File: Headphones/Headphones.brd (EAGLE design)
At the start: 50 x 50 mm, 26 parts, among them U1 SI4468, Y1 30MHz

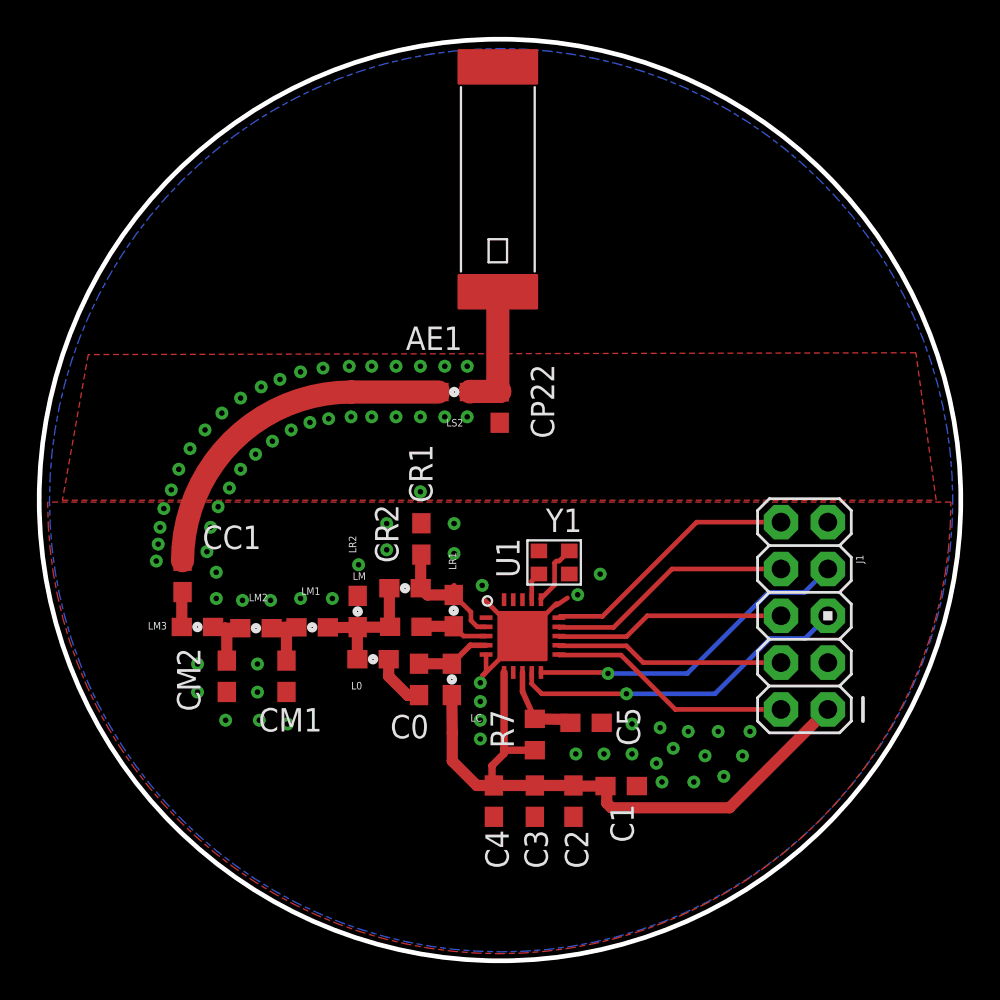
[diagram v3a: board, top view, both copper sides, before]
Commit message: Fixed antenna and transciever stop masks. Finished via placement. DRC checks out
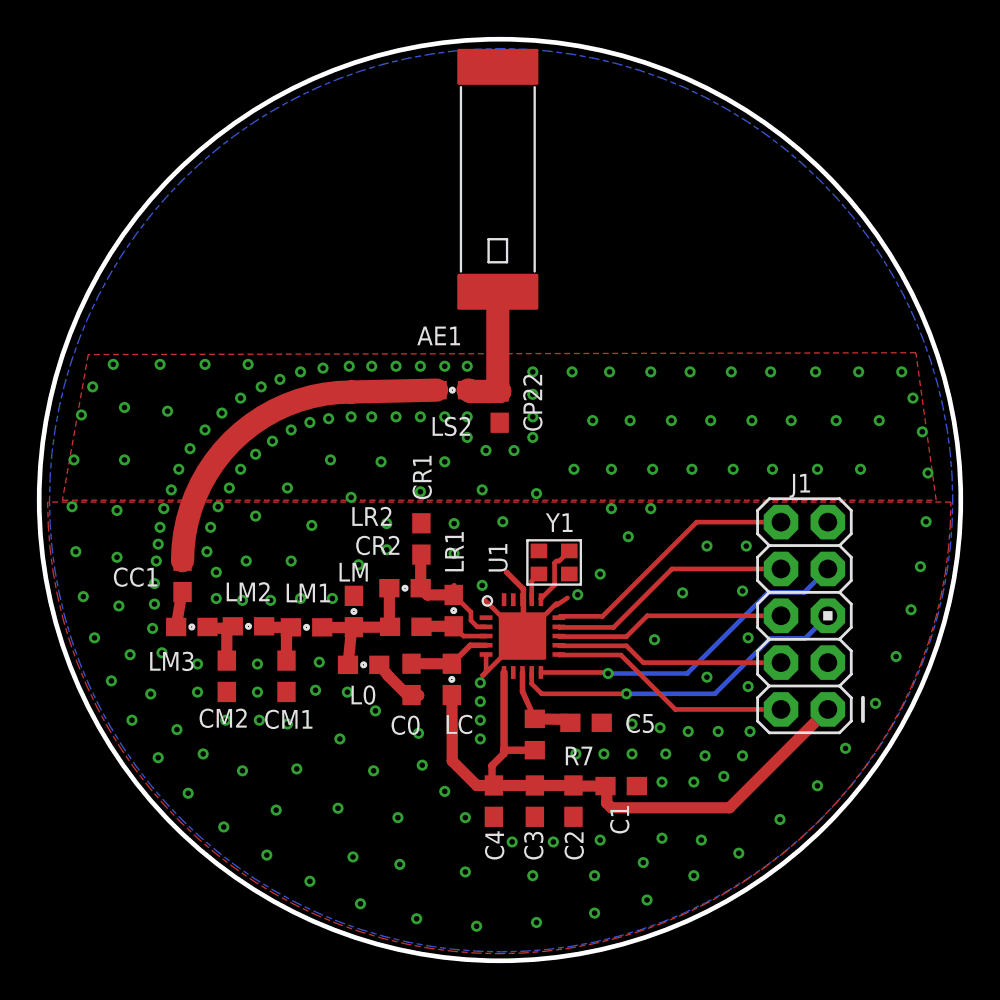
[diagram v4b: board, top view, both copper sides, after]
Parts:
- moved L0 0.59 mm to (23.6, 13.5)
- moved LM2 0.42 mm to (17.4, 15.6)
- moved C0 0.41 mm to (26.2, 12.7)
- moved LM1 0.30 mm to (20.5, 15.5)
- moved LM3 0.30 mm to (14.3, 15.5)
- moved LM 0.20 mm to (23.1, 16.4)
- moved LS2 0.14 mm to (28.5, 28.4)
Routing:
- net GND: track 7.33 -> 10.0 mm, vias 77 -> 208
- net N$6: track 7.23 -> 7.84 mm
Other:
- board text added: "3V3"
- board text added: "GND"
- board text added: "GP0"
- board text added: "GP1"
- board text added: "NIRQ"
- board text added: "NSEL"
- board text added: "SCLK"
- board text added: "SDI"
- board text added: "SDO"

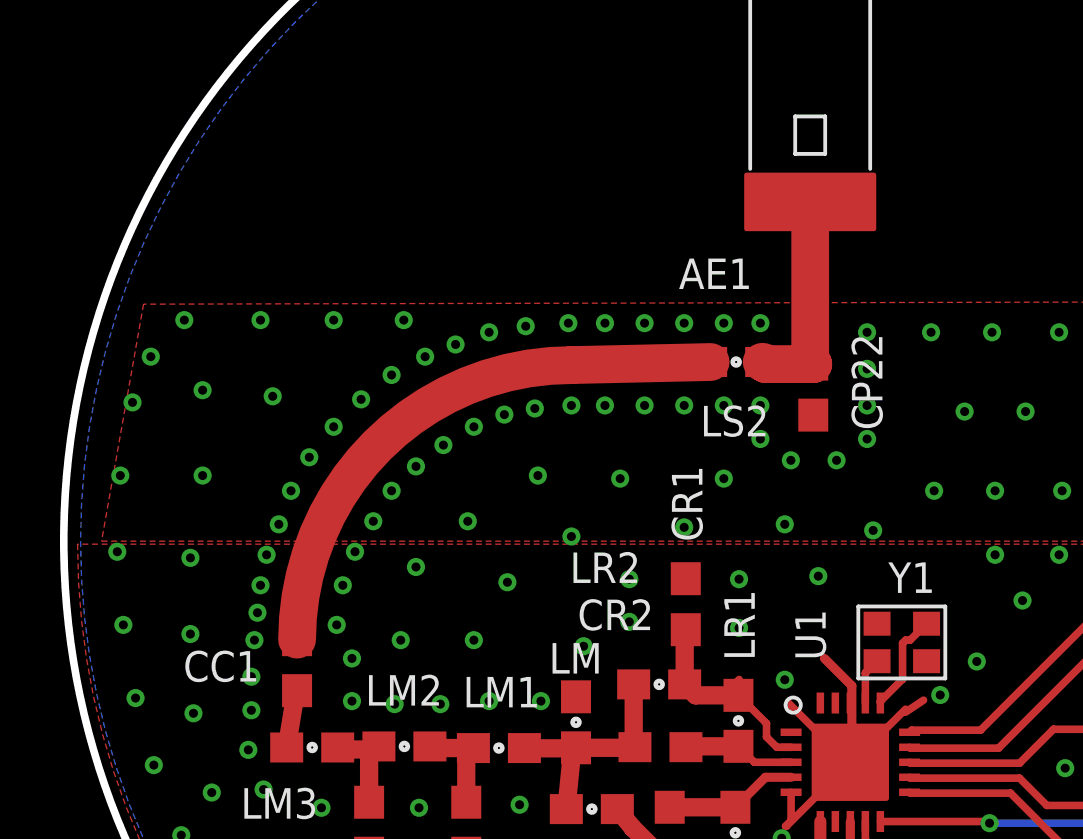
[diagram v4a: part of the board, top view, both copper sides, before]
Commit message: Minor routing changes to antenna
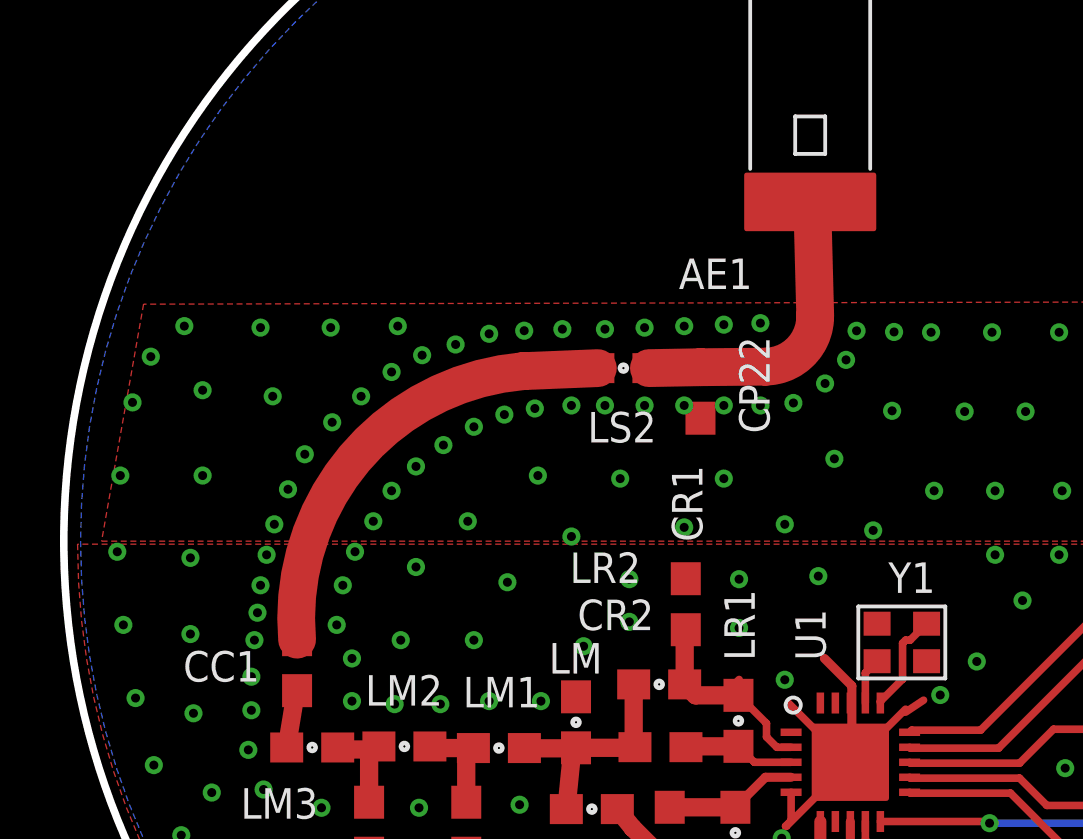
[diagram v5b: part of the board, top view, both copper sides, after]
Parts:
- moved LS2 3.76 mm to (24.7, 28.2)
- moved CP22 3.76 mm to (27.3, 27.3)
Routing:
- net N$9: track 17.6 -> 14.2 mm
- net N$13: track 7.29 -> 10.2 mm
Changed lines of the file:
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@@
 <setting verticaltext="up"/>
 </settings>
-<grid distance="4" unitdist="mil" unit="mm" style="lines" multiple="1" display="yes" altdistance="0.025" altunitdist="inch" altunit="inch"/>
+<grid distance="0.05" unitdist="mm" unit="mm" style="lines" multiple="1" display="yes" altdistance="0.025" altunitdist="inch" altunit="inch"/>
 <layers>
 <layer number="1" name="Top" color="4" fill="1" visible="yes" active="yes"/>
@@
 <attribute name="NAME" x="23.9918" y="19.004" size="1.016" layer="25" font="vector" ratio="14" rot="R180"/>
 </element>
-<element name="LS2" library="SparkFun-Passives" package="0603" value="10nH" x="28.4534" y="28.3716" smashed="yes" rot="R180">
-<attribute name="NAME" x="29.552" y="26.9096" size="1.016" layer="25" font="vector" ratio="14" rot="R180"/>
-</element>
-<element name="CP22" library="resistor" package="C0603" value="1.2pF" x="31.023" y="27.452" smashed="yes" rot="R90">
-<attribute name="NAME" x="33.328" y="26.097" size="1.016" layer="25" ratio="14" rot="R90"/>
+<element name="LS2" library="SparkFun-Passives" package="0603" value="10nH" x="24.6942" y="28.1684" smashed="yes" rot="R180">
+<attribute name="NAME" x="25.7928" y="26.7064" size="1.016" layer="25" font="vector" ratio="14" rot="R180"/>
+</element>
+<element name="CP22" library="resistor" package="C0603" value="1.2pF" x="27.2638" y="27.3488" smashed="yes" rot="R90">
+<attribute name="NAME" x="29.5688" y="25.9938" size="1.016" layer="25" ratio="14" rot="R90"/>
 </element>
 </elements>
@@
 <via x="29.2608" y="26.924" extent="1-16" drill="0.3"/>
 <via x="29.2608" y="29.6672" extent="1-16" drill="0.3"/>
-<via x="28.0416" y="29.6672" extent="1-16" drill="0.3"/>
-<via x="26.7208" y="29.6672" extent="1-16" drill="0.3"/>
-<via x="25.4" y="29.6672" extent="1-16" drill="0.3"/>
-<via x="24.0792" y="29.6672" extent="1-16" drill="0.3"/>
-<via x="22.86" y="29.6672" extent="1-16" drill="0.3"/>
-<via x="21.4376" y="29.5656" extent="1-16" drill="0.3"/>
-<via x="20.2184" y="29.3624" extent="1-16" drill="0.3"/>
+<via x="28.0416" y="29.6172" extent="1-16" drill="0.3"/>
+<via x="26.7208" y="29.5672" extent="1-16" drill="0.3"/>
+<via x="25.4" y="29.5172" extent="1-16" drill="0.3"/>
+<via x="24.0792" y="29.4672" extent="1-16" drill="0.3"/>
+<via x="22.66" y="29.4672" extent="1-16" drill="0.3"/>
+<via x="21.3876" y="29.4156" extent="1-16" drill="0.3"/>
+<via x="20.2184" y="29.3124" extent="1-16" drill="0.3"/>
 <via x="19.1008" y="28.956" extent="1-16" drill="0.3"/>
-<via x="18.0848" y="28.5496" extent="1-16" drill="0.3"/>
-<via x="16.9672" y="27.94" extent="1-16" drill="0.3"/>
-<via x="15.9512" y="27.1272" extent="1-16" drill="0.3"/>
-<via x="15.0368" y="26.2128" extent="1-16" drill="0.3"/>
-<via x="14.224" y="25.1968" extent="1-16" drill="0.3"/>
-<via x="13.6144" y="24.0792" extent="1-16" drill="0.3"/>
-<via x="13.208" y="22.9616" extent="1-16" drill="0.3"/>
+<via x="17.9848" y="28.5996" extent="1-16" drill="0.3"/>
+<via x="16.9672" y="28.04" extent="1-16" drill="0.3"/>
+<via x="15.9512" y="27.2272" extent="1-16" drill="0.3"/>
+<via x="14.9868" y="26.3628" extent="1-16" drill="0.3"/>
+<via x="14.074" y="25.2968" extent="1-16" drill="0.3"/>
+<via x="13.5144" y="24.1292" extent="1-16" drill="0.3"/>
+<via x="13.058" y="22.9616" extent="1-16" drill="0.3"/>
 <via x="12.8016" y="21.9456" extent="1-16" drill="0.3"/>
 <via x="12.5984" y="20.9296" extent="1-16" drill="0.3"/>
@@
 <via x="19.5072" y="10.2616" extent="1-16" drill="0.3"/>
 <via x="17.9832" y="10.4648" extent="1-16" drill="0.3"/>
-<via x="29.2608" y="25.8064" extent="1-16" drill="0.3"/>
-<via x="30.2768" y="25.0952" extent="1-16" drill="0.3"/>
-<via x="31.8008" y="25.0952" extent="1-16" drill="0.3"/>
-<via x="32.8168" y="25.8064" extent="1-16" drill="0.3"/>
-<via x="32.8168" y="26.924" extent="1-16" drill="0.3"/>
-<via x="32.8168" y="28.1432" extent="1-16" drill="0.3"/>
-<via x="32.8168" y="29.3624" extent="1-16" drill="0.3"/>
+<via x="30.3608" y="27.0064" extent="1-16" drill="0.3"/>
+<via x="31.7268" y="25.1452" extent="1-16" drill="0.3"/>
+<via x="33.6508" y="26.7452" extent="1-16" drill="0.3"/>
+<via x="31.4168" y="27.6564" extent="1-16" drill="0.3"/>
+<via x="33.7168" y="29.374" extent="1-16" drill="0.3"/>
+<via x="32.1168" y="28.4432" extent="1-16" drill="0.3"/>
+<via x="32.4668" y="29.4124" extent="1-16" drill="0.3"/>
 <via x="34.9504" y="29.3624" extent="1-16" drill="0.3"/>
 <via x="36.9824" y="29.3624" extent="1-16" drill="0.3"/>
@@
 <via x="44.3992" y="19.9136" extent="1-16" drill="0.3"/>
 <via x="42.2656" y="12.8016" extent="1-16" drill="0.3"/>
-<via x="17.3736" y="29.7688" extent="1-16" drill="0.3"/>
-<via x="15.0368" y="29.7688" extent="1-16" drill="0.3"/>
-<via x="12.5984" y="29.7688" extent="1-16" drill="0.3"/>
-<via x="10.0584" y="29.7688" extent="1-16" drill="0.3"/>
+<via x="17.1736" y="29.5688" extent="1-16" drill="0.3"/>
+<via x="14.9368" y="29.5188" extent="1-16" drill="0.3"/>
+<via x="12.5984" y="29.5188" extent="1-16" drill="0.3"/>
+<via x="10.0584" y="29.5688" extent="1-16" drill="0.3"/>
 <via x="8.9408" y="28.5496" extent="1-16" drill="0.3"/>
 <via x="8.3312" y="27.0256" extent="1-16" drill="0.3"/>
@@
 <contactref element="LS2" pad="2"/>
 <contactref element="CC1" pad="1"/>
-<wire x1="13.817" y1="19.117" x2="22.97" y2="28.27" width="1.26" layer="1" curve="-90"/>
-<wire x1="22.97" y1="28.27" x2="27.6034" y2="28.3716" width="1.26" layer="1"/>
+<wire x1="13.817" y1="19.117" x2="21.3444" y2="28.0668" width="1.26" layer="1" curve="-90"/>
+<wire x1="21.3444" y1="28.0668" x2="23.8442" y2="28.1684" width="1.26" layer="1"/>
 </signal>
 <signal name="N$13">
@@
 <contactref element="AE1" pad="1"/>
 <contactref element="CP22" pad="2"/>
-<wire x1="29.3034" y1="28.3716" x2="29.437" y2="28.302" width="1.259840625" layer="1" curve="-90"/>
-<wire x1="29.437" y1="28.302" x2="31.023" y2="28.302" width="1.259840625" layer="1"/>
-<wire x1="31.023" y1="28.302" x2="30.921" y2="28.404" width="1.259840625" layer="1" curve="-90"/>
-<wire x1="30.921" y1="28.404" x2="30.921" y2="33.809" width="1.259840625" layer="1"/>
+<wire x1="29.4392" y1="28.2168" x2="31.088" y2="29.9156" width="1.26" layer="1" curve="90"/>
+<wire x1="31.088" y1="29.9156" x2="30.988" y2="33.742" width="1.26" layer="1"/>
+<wire x1="30.988" y1="33.742" x2="30.921" y2="33.809" width="1.26" layer="1" curve="90"/>
+<wire x1="25.5442" y1="28.1684" x2="27.2638" y2="28.1988" width="1.26" layer="1"/>
+<wire x1="27.2638" y1="28.1988" x2="29.4392" y2="28.2168" width="1.26" layer="1"/>
 </signal>
 </signals>

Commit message: More fixes
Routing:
- net GND: vias 208 -> 214
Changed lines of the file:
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@@
 </polygon>
 <wire x1="34.1" y1="16.7" x2="34.7" y2="17.1" width="0.254" layer="1"/>
-<via x="15.1384" y="19.6088" extent="1-16" drill="0.3"/>
-<via x="15.3416" y="20.9296" extent="1-16" drill="0.3"/>
-<via x="15.748" y="22.0472" extent="1-16" drill="0.3"/>
-<via x="16.3576" y="23.0632" extent="1-16" drill="0.3"/>
-<via x="16.9672" y="24.0792" extent="1-16" drill="0.3"/>
-<via x="17.78" y="24.892" extent="1-16" drill="0.3"/>
-<via x="18.6944" y="25.6032" extent="1-16" drill="0.3"/>
-<via x="19.7104" y="26.2128" extent="1-16" drill="0.3"/>
+<via x="15.1884" y="19.4088" extent="1-16" drill="0.3"/>
+<via x="15.2916" y="21.3296" extent="1-16" drill="0.3"/>
+<via x="15.498" y="22.3472" extent="1-16" drill="0.3"/>
+<via x="16.0576" y="23.2132" extent="1-16" drill="0.3"/>
+<via x="16.8172" y="24.2792" extent="1-16" drill="0.3"/>
+<via x="17.58" y="25.092" extent="1-16" drill="0.3"/>
+<via x="18.4444" y="25.7532" extent="1-16" drill="0.3"/>
+<via x="19.5604" y="26.3128" extent="1-16" drill="0.3"/>
 <via x="20.7264" y="26.6192" extent="1-16" drill="0.3"/>
 <via x="21.7424" y="26.8224" extent="1-16" drill="0.3"/>
 <via x="22.9616" y="26.924" extent="1-16" drill="0.3"/>
-<via x="24.0792" y="26.924" extent="1-16" drill="0.3"/>
-<via x="25.4" y="26.924" extent="1-16" drill="0.3"/>
+<via x="24.0792" y="26.824" extent="1-16" drill="0.3"/>
+<via x="25.9" y="26.824" extent="1-16" drill="0.3"/>
 <via x="29.972" y="12.4968" extent="1-16" drill="0.3"/>
 <via x="29.972" y="11.4808" extent="1-16" drill="0.3"/>
 <via x="29.972" y="10.4648" extent="1-16" drill="0.3"/>
 <via x="29.972" y="9.4488" extent="1-16" drill="0.3"/>
-<via x="26.7208" y="26.924" extent="1-16" drill="0.3"/>
-<via x="28.0416" y="26.924" extent="1-16" drill="0.3"/>
-<via x="29.2608" y="26.924" extent="1-16" drill="0.3"/>
+<wire x1="26.7208" y1="26.924" x2="26.7208" y2="26.924" width="0" layer="19" extent="1-16"/>
+<wire x1="28.0416" y1="26.924" x2="28.0416" y2="26.924" width="0" layer="19" extent="1-16"/>
+<via x="28.5608" y="26.824" extent="1-16" drill="0.3"/>
 <via x="29.2608" y="29.6672" extent="1-16" drill="0.3"/>
 <via x="28.0416" y="29.6172" extent="1-16" drill="0.3"/>
 <via x="26.7208" y="29.5672" extent="1-16" drill="0.3"/>
 <via x="25.4" y="29.5172" extent="1-16" drill="0.3"/>
-<via x="24.0792" y="29.4672" extent="1-16" drill="0.3"/>
+<via x="24.0792" y="29.5172" extent="1-16" drill="0.3"/>
 <via x="22.66" y="29.4672" extent="1-16" drill="0.3"/>
 <via x="21.3876" y="29.4156" extent="1-16" drill="0.3"/>
@@
 <via x="19.5072" y="10.2616" extent="1-16" drill="0.3"/>
 <via x="17.9832" y="10.4648" extent="1-16" drill="0.3"/>
-<via x="30.3608" y="27.0064" extent="1-16" drill="0.3"/>
+<via x="29.7608" y="26.9064" extent="1-16" drill="0.3"/>
 <via x="31.7268" y="25.1452" extent="1-16" drill="0.3"/>
 <via x="33.6508" y="26.7452" extent="1-16" drill="0.3"/>
@@
 <via x="33.02" y="22.7584" extent="1-16" drill="0.3"/>
 <via x="30.0736" y="22.9616" extent="1-16" drill="0.3"/>
-<via x="28.0416" y="24.4856" extent="1-16" drill="0.3"/>
+<via x="28.7416" y="25.5356" extent="1-16" drill="0.3"/>
 <via x="24.5872" y="24.4856" extent="1-16" drill="0.3"/>
 <via x="21.844" y="24.5872" extent="1-16" drill="0.3"/>
-<via x="19.5072" y="23.0632" extent="1-16" drill="0.3"/>
-<via x="17.78" y="21.5392" extent="1-16" drill="0.3"/>
+<via x="18.8572" y="23.6632" extent="1-16" drill="0.3"/>
+<via x="17.08" y="21.6892" extent="1-16" drill="0.3"/>
 <via x="17.272" y="19.1008" extent="1-16" drill="0.3"/>
 <via x="19.7104" y="19.1008" extent="1-16" drill="0.3"/>
@@
 <wire x1="34.1" y1="16.7" x2="34.1" y2="16.8" width="0" layer="19" extent="1-1"/>
 <wire x1="32.259" y1="17.005" x2="32.3088" y2="17.5768" width="0" layer="19" extent="1-1"/>
+<via x="30.6608" y="27.1564" extent="1-16" drill="0.3"/>
+<via x="25.0292" y="26.774" extent="1-16" drill="0.3"/>
+<via x="25.9792" y="25.674" extent="1-16" drill="0.3"/>
+<via x="27.2792" y="25.124" extent="1-16" drill="0.3"/>
+<via x="28.7736" y="24.0116" extent="1-16" drill="0.3"/>
+<via x="15.28" y="20.3892" extent="1-16" drill="0.3"/>
+<via x="20.7572" y="22.9632" extent="1-16" drill="0.3"/>
+<via x="18.9072" y="21.2132" extent="1-16" drill="0.3"/>
 </signal>
 <signal name="N$7">
